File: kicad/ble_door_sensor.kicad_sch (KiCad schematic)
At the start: 40 parts, among them J1 Prog Header, J101 Conn_01x08, Q1 Photo, SW101 SW_Reed, SW102 SW_Push, T1 ToolingHole, T2 ToolingHole, T3 ToolingHole, U1 nRF52832-QFxx, U101 TMP100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

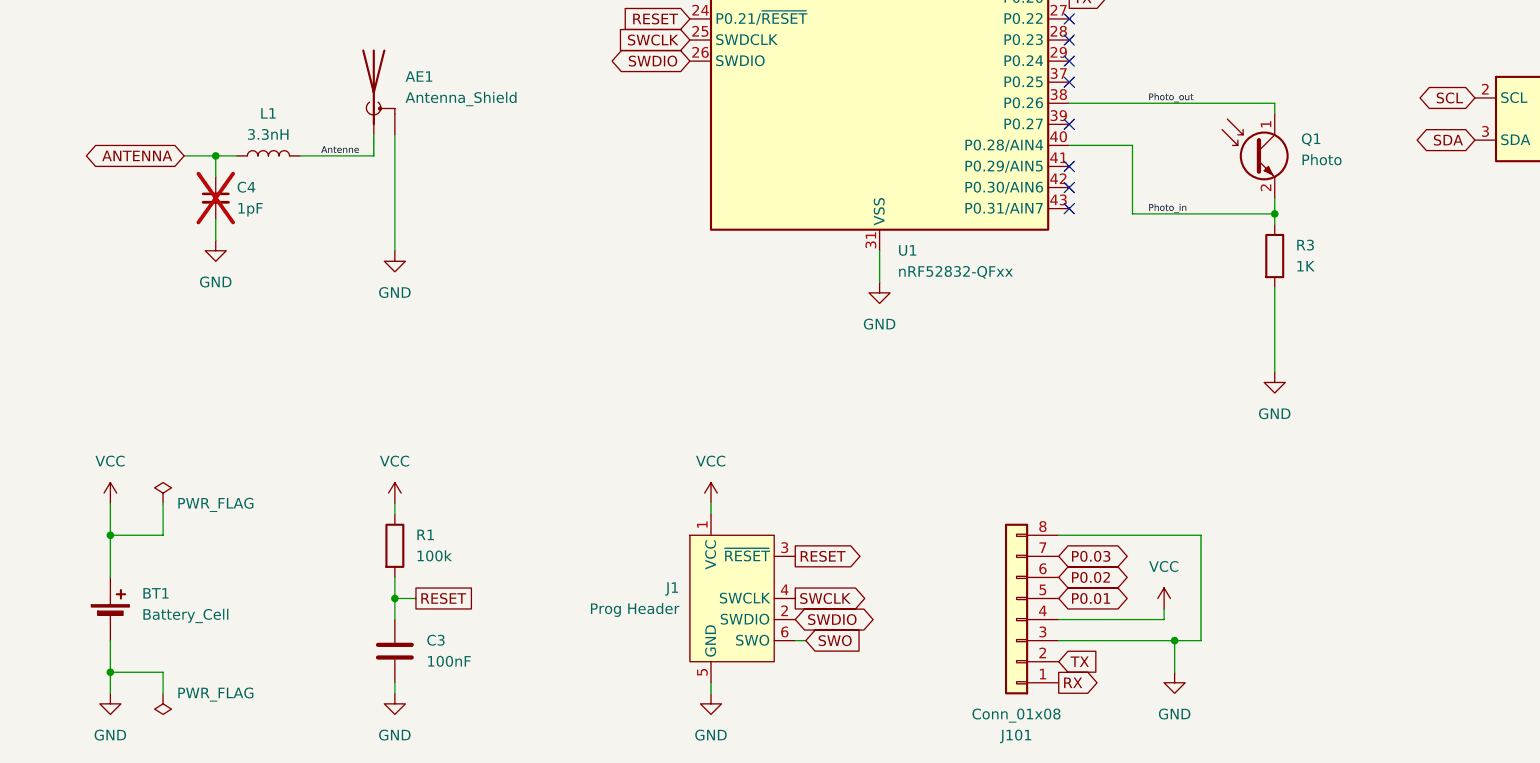
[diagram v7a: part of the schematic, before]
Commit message: Add MPN and Manufacturer for most parts
To be able to order from different houses
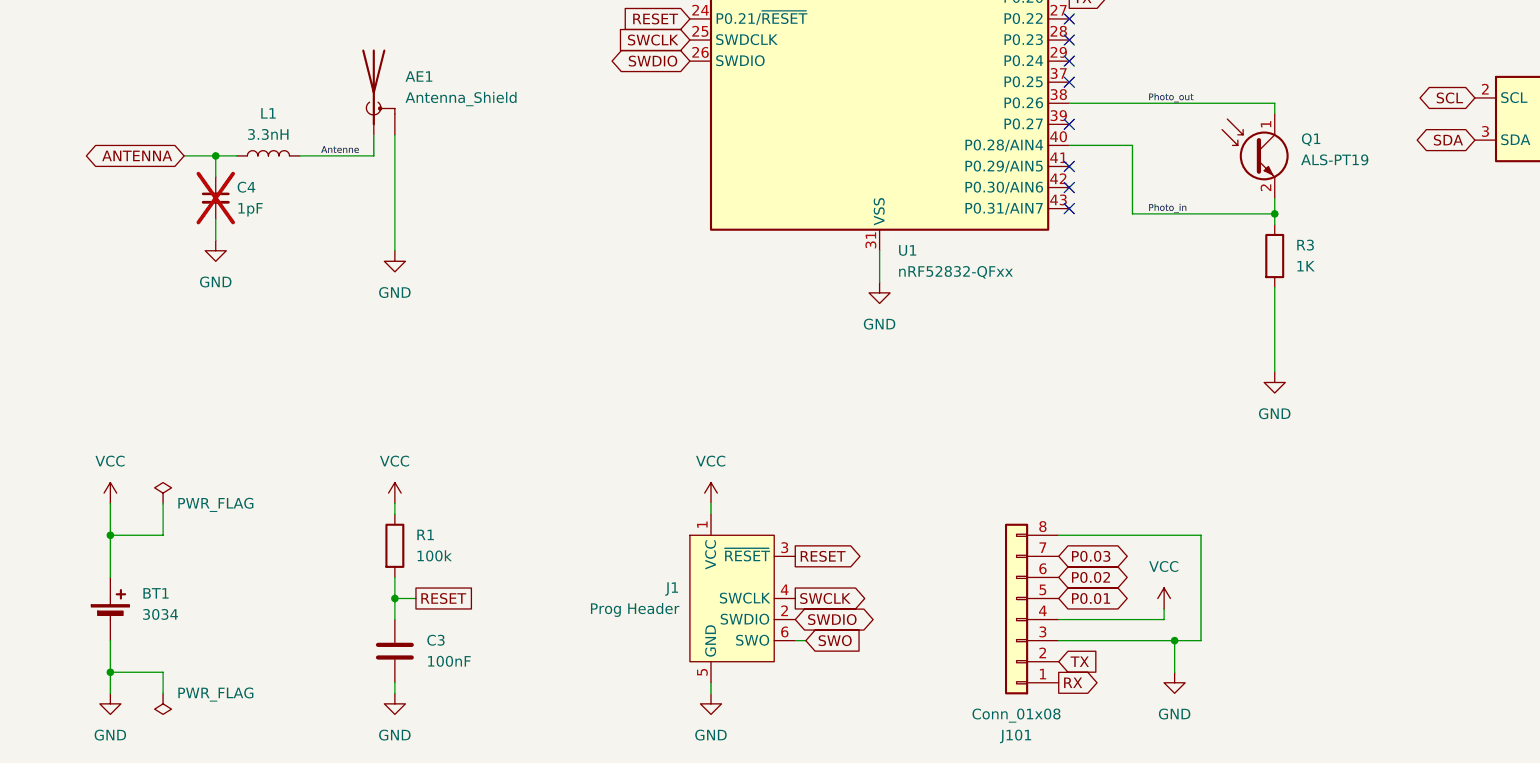
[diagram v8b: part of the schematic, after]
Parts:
- AE1, C4, H101, H102, J1, J101, SW101, T1, T2, T3: MPN (none) -> -
- BT1: value Battery_Cell -> 3034; MPN (none) -> 3034TR; Manufacturer (none) -> Keystone
- C1, C101, C107, C11, C3: MPN (none) -> 100nF 0402
- C13: MPN (none) -> 10nF 0402
- C2: MPN (none) -> 4,7uF 0603
- C5: MPN (none) -> 1uF 0603
- C6, C8: MPN (none) -> 12pF 0402
- C7, C9: MPN (none) -> 100pF 0402
- D101: MPN (none) -> KP-1608SGC
- L1: MPN (none) -> LQG15HS3N3C02D; Manufacturer (none) -> Murata Electronics
- L101: MPN (none) -> LQW15AN15NH00D; Manufacturer (none) -> Murata Electronics
- L102: MPN (none) -> MLZ1608E100MT; Manufacturer (none) -> TDK
- Q1: value Photo -> ALS-PT19; MPN (none) -> ALS-PT19-315C/L177/TR8
- R1, R101, R104, R105: MPN (none) -> 100K
- R102, R3: MPN (none) -> 1K
- R2: MPN (none) -> 1M
- SW102: MPN (none) -> TS-1187A-B-A-B; Manufacturer (none) -> XKB Connectivity
- U1: MPN (none) -> NRF52832-QFAA-R; Manufacturer (none) -> Nordic Semicon
- U101: MPN (none) -> TMP100NA/3K; Manufacturer (none) -> Texas Instruments
- U2: MPN (none) -> SHTC3-TR-10KS; Manufacturer (none) -> Sensirion
- Y1: MPN (none) -> X322532MOB4SI; Manufacturer (none) -> YXC
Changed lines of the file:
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@@
+      (effects (font (size 1.27 1.27)) hide)
+    )
+    (property "MPN" "-" (at 237.49 151.13 0)
       (effects (font (size 1.27 1.27)) hide)
     )
@@
       (effects (font (size 1.27 1.27)) hide)
     )
+    (property "MPN" "LQG15HS3N3C02D" (at 52.07 119.38 0)
+      (effects (font (size 1.27 1.27)) hide)
+    )
+    (property "Manufacturer" "Murata Electronics" (at 52.07 119.38 0)
+      (effects (font (size 1.27 1.27)) hide)
+    )
     (pin "2")
     (pin "1")
@@
     )
     (property "LCSC#" "-" (at 142.24 175.26 0)
+      (effects (font (size 1.27 1.27)) hide)
+    )
+    (property "MPN" "-" (at 142.24 175.26 0)
       (effects (font (size 1.27 1.27)) hide)
     )
@@
       (effects (font (size 1.27 1.27)) hide)
     )
+    (property "MPN" "-" (at 248.92 54.61 0)
+      (effects (font (size 1.27 1.27)) hide)
+    )
     (pin "2")
     (pin "1")
@@
       (effects (font (size 1.27 1.27)) hide)
     )
+    (property "MPN" "-" (at 215.9 158.75 0)
+      (effects (font (size 1.27 1.27)) hide)
+    )
     (instances
       (project "ble_door_sensor"
@@
       (effects (font (size 1.27 1.27)) (justify left))
     )
-    (property "Value" "Photo" (at 176.53 119.9007 0)
+    (property "Value" "ALS-PT19" (at 176.53 119.9007 0)
       (effects (font (size 1.27 1.27)) (justify left))
     )
@@
       (effects (font (size 1.27 1.27)) hide)
     )
+    (property "MPN" "ALS-PT19-315C/L177/TR8" (at 170.815 119.38 0)
+      (effects (font (size 1.27 1.27)) hide)
+    )
     (pin "2")
     (pin "1")
@@
     )
     (property "LCSC#" "C25741" (at 67.31 166.37 0)
+      (effects (font (size 1.27 1.27)) hide)
+    )
+    (property "MPN" "100K" (at 67.31 166.37 0)
       (effects (font (size 1.27 1.27)) hide)
     )
@@
       (effects (font (size 1.27 1.27)) hide)
     )
+    (property "MPN" "100nF 0402" (at 34.29 45.72 0)
+      (effects (font (size 1.27 1.27)) hide)
+    )
     (pin "1")
     (pin "2")
@@
     )
     (property "LCSC#" "C1525" (at 24.13 45.72 0)
+      (effects (font (size 1.27 1.27)) hide)
+    )
+    (property "MPN" "100nF 0402" (at 24.13 45.72 0)
       (effects (font (size 1.27 1.27)) hide)
     )
@@
       (effects (font (size 1.27 1.27)) hide)
     )
+    (property "MPN" "TS-1187A-B-A-B" (at 205.74 55.245 0)
+      (effects (font (size 1.27 1.27)) hide)
+    )
+    (property "Manufacturer" "XKB Connectivity" (at 205.74 55.245 0)
+      (effects (font (size 1.27 1.27)) hide)
+    )
     (pin "2")
     (pin "1")
@@
       (effects (font (size 1.27 1.27)) (justify left))
     )
-    (property "Value" "Battery_Cell" (at 36.83 174.6885 0)
+    (property "Value" "3034" (at 36.83 174.6885 0)
       (effects (font (size 1.27 1.27)) (justify left))
     )
@@
       (effects (font (size 1.27 1.27)) hide)
     )
+    (property "MPN" "3034TR" (at 33.02 175.26 0)
+      (effects (font (size 1.27 1.27)) hide)
+    )
+    (property "Manufacturer" "Keystone" (at 33.02 175.26 0)
+      (effects (font (size 1.27 1.27)) hide)
+    )
     (pin "2")
     (pin "1")
@@
       (effects (font (size 1.27 1.27)) hide)
     )
+    (property "MPN" "100nF 0402" (at 86.36 45.72 0)
+      (effects (font (size 1.27 1.27)) hide)
+    )
     (pin "2")
     (pin "1")
@@
       (effects (font (size 1.27 1.27)) hide)
     )
+    (property "MPN" "1K" (at 173.355 131.445 0)
+      (effects (font (size 1.27 1.27)) hide)
+    )
     (pin "1")
     (pin "2")
@@
       (effects (font (size 1.27 1.27)) hide)
     )
+    (property "MPN" "MLZ1608E100MT" (at 128.27 22.86 0)
+      (effects (font (size 1.27 1.27)) hide)
+    )
+    (property "Manufacturer" "TDK" (at 128.27 22.86 0)
+      (effects (font (size 1.27 1.27)) hide)
+    )
     (pin "2")
     (pin "1")
@@
     )
     (property "LCSC#" "C2880044" (at 205.105 114.935 0)
+      (effects (font (size 1.27 1.27)) hide)
+    )
+    (property "MPN" "SHTC3-TR-10KS" (at 205.105 114.935 0)
+      (effects (font (size 1.27 1.27)) hide)
+    )
+    (property "Manufacturer" "Sensirion" (at 205.105 114.935 0)
       (effects (font (size 1.27 1.27)) hide)
     )
@@
       (effects (font (size 1.27 1.27)) hide)
     )
+    (property "MPN" "1K" (at 180.975 38.735 0)
+      (effects (font (size 1.27 1.27)) hide)
+    )
     (pin "1")
     (pin "2")
@@
       (effects (font (size 1.27 1.27)) hide)
     )
+    (property "MPN" "1uF 0603" (at 54.61 45.72 0)
+      (effects (font (size 1.27 1.27)) hide)
+    )
     (pin "1")
     (pin "2")
@@
     )
     (property "LCSC#" "C1547" (at 59.69 92.71 90)
+      (effects (font (size 1.27 1.27)) hide)
+    )
+    (property "MPN" "12pF 0402" (at 59.69 92.71 0)
       (effects (font (size 1.27 1.27)) hide)
     )
@@
       (effects (font (size 1.27 1.27)) hide)
     )
+    (property "MPN" "-" (at 257.81 151.13 0)
+      (effects (font (size 1.27 1.27)) hide)
+    )
     (instances
       (project "ble_door_sensor"
@@
     )
     (property "LCSC#" "C1546" (at 64.77 45.72 0)
+      (effects (font (size 1.27 1.27)) hide)
+    )
+    (property "MPN" "100pF 0402" (at 64.77 45.72 0)
       (effects (font (size 1.27 1.27)) hide)
     )
@@
       (effects (font (size 1.27 1.27)) hide)
     )
+    (property "MPN" "10nF 0402" (at 257.81 54.61 0)
+      (effects (font (size 1.27 1.27)) hide)
+    )
     (pin "2")
     (pin "1")
@@
     )
     (property "LCSC#" "C31810" (at 261.62 118.11 0)
+      (effects (font (size 1.27 1.27)) hide)
+    )
+    (property "MPN" "TMP100NA/3K" (at 261.62 118.11 0)
+      (effects (font (size 1.27 1.27)) hide)
+    )
+    (property "Manufacturer" "Texas Instruments" (at 261.62 118.11 0)
       (effects (font (size 1.27 1.27)) hide)
     )
@@
       (effects (font (size 1.27 1.27)) hide)
     )
+    (property "MPN" "12pF 0402" (at 66.04 82.55 0)
+      (effects (font (size 1.27 1.27)) hide)
+    )
     (pin "2")
     (pin "1")
@@
     )
     (property "LCSC#" "C19666" (at 44.45 45.72 0)
+      (effects (font (size 1.27 1.27)) hide)
+    )
+    (property "MPN" "4,7uF 0603" (at 44.45 45.72 0)
       (effects (font (size 1.27 1.27)) hide)
     )
@@
       (effects (font (size 1.27 1.27)) hide)
     )
+    (property "MPN" "100K" (at 215.9 41.275 0)
+      (effects (font (size 1.27 1.27)) hide)
+    )
     (pin "2")
     (pin "1")
@@
     )
     (property "LCSC#" "C77540" (at 125.73 87.63 0)
+      (effects (font (size 1.27 1.27)) hide)
+    )
+    (property "MPN" "NRF52832-QFAA-R" (at 125.73 87.63 0)
+      (effects (font (size 1.27 1.27)) hide)
+    )
+    (property "Manufacturer" "Nordic Semicon" (at 125.73 87.63 0)
       (effects (font (size 1.27 1.27)) hide)
     )
@@
       (effects (font (size 1.27 1.27)) hide)
     )
+    (property "MPN" "LQW15AN15NH00D" (at 115.57 22.86 0)
+      (effects (font (size 1.27 1.27)) hide)
+    )
+    (property "Manufacturer" "Murata Electronics" (at 115.57 22.86 0)
+      (effects (font (size 1.27 1.27)) hide)
+    )
     (pin "2")
     (pin "1")
@@
     )
     (property "LCSC#" "C1525" (at 215.9 55.245 0)
+      (effects (font (size 1.27 1.27)) hide)
+    )
+    (property "MPN" "100nF 0402" (at 215.9 55.245 0)
       (effects (font (size 1.27 1.27)) hide)
     )
@@
       (effects (font (size 1.27 1.27)) hide)
     )
+    (property "MPN" "-" (at 215.9 151.13 0)
+      (effects (font (size 1.27 1.27)) hide)
+    )
     (instances
       (project "ble_door_sensor"
@@
       (effects (font (size 1.27 1.27)) hide)
     )
+    (property "MPN" " KP-1608SGC" (at 180.975 50.165 0)
+      (effects (font (size 1.27 1.27)) hide)
+    )
     (pin "2")
     (pin "1")
@@
     )
     (property "LCSC#" "C25741" (at 236.22 107.95 0)
+      (effects (font (size 1.27 1.27)) hide)
+    )
+    (property "MPN" "100K" (at 236.22 107.95 0)
       (effects (font (size 1.27 1.27)) hide)
     )
@@
       (effects (font (size 1.27 1.27)) hide)
     )
+    (property "MPN" "-" (at 107.95 172.72 0)
+      (effects (font (size 1.27 1.27)) hide)
+    )
     (pin "6")
     (pin "1")
@@
       (effects (font (size 1.27 1.27)) hide)
     )
+    (property "MPN" "-" (at 45.72 124.46 0)
+      (effects (font (size 1.27 1.27)) hide)
+    )
     (pin "1")
     (pin "2")
@@
       (effects (font (size 1.27 1.27)) hide)
     )
+    (property "MPN" "1M" (at 257.81 39.37 0)
+      (effects (font (size 1.27 1.27)) hide)
+    )
     (pin "2")
     (pin "1")
@@
     )
     (property "LCSC#" "C1546" (at 74.93 45.72 0)
+      (effects (font (size 1.27 1.27)) hide)
+    )
+    (property "MPN" "100pF 0402" (at 74.93 45.72 0)
       (effects (font (size 1.27 1.27)) hide)
     )
@@
       (effects (font (size 1.27 1.27)) hide)
     )
+    (property "MPN" "-" (at 237.49 158.75 0)
+      (effects (font (size 1.27 1.27)) hide)
+    )
     (instances
       (project "ble_door_sensor"
@@
     )
     (property "LCSC#" "C1525" (at 67.31 179.07 0)
+      (effects (font (size 1.27 1.27)) hide)
+    )
+    (property "MPN" "100nF 0402" (at 67.31 179.07 0)
       (effects (font (size 1.27 1.27)) hide)
     )
@@
       (effects (font (size 1.27 1.27)) hide)
     )
+    (property "MPN" "-" (at 64.77 111.76 0)
+      (effects (font (size 1.27 1.27)) hide)
+    )
     (pin "1")
     (pin "2")
@@
       (effects (font (size 1.27 1.27)) hide)
     )
+    (property "MPN" "X322532MOB4SI" (at 77.47 87.63 0)
+      (effects (font (size 1.27 1.27)) hide)
+    )
+    (property "Manufacturer" "YXC" (at 77.47 87.63 0)
+      (effects (font (size 1.27 1.27)) hide)
+    )
     (pin "1")
     (pin "2")
@@
       (effects (font (size 1.27 1.27)) hide)
     )
+    (property "MPN" "100K" (at 246.38 107.95 0)
+      (effects (font (size 1.27 1.27)) hide)
+    )
